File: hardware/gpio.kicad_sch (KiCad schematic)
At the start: 12 parts, among them J8 UART, J9 GPIO, Q4 BSN20

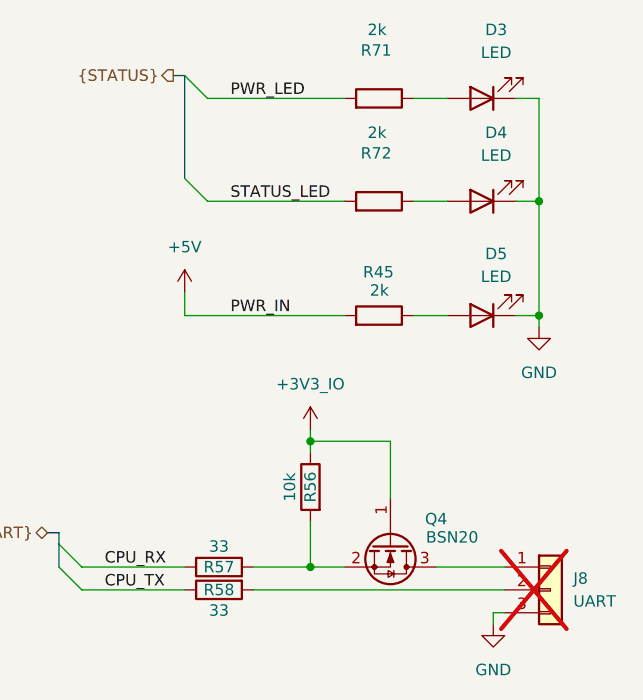
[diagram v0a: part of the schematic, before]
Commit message: Update crystal
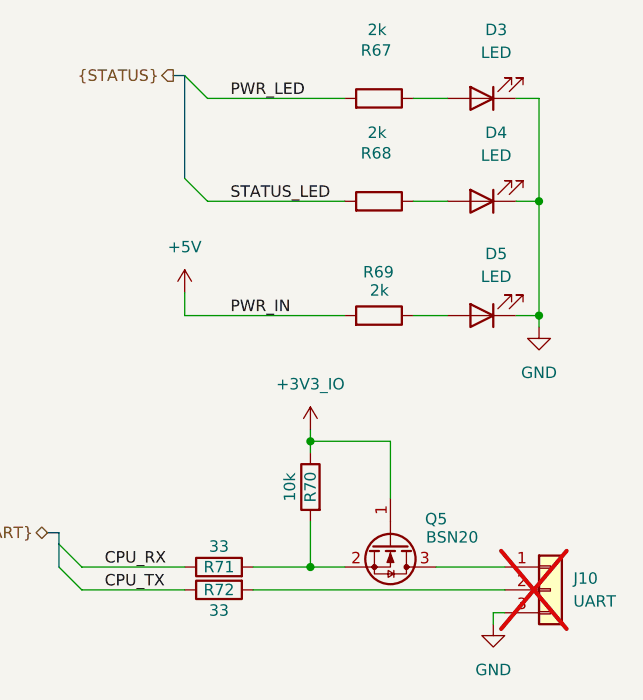
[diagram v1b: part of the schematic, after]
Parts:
- renumbered J8 to J10, Q4 to Q5, R71 to R67, R72 to R68, R45 to R69, R56 to R70, R57 to R71, R58 to R72
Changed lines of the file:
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@@
 		(on_board yes)
 		(dnp no)
-		(property "Reference" "R56"
+		(property "Reference" "R70"
 			(at 170.18 120.65 90)
 			(effects
@@
 			(project "cm0"
 				(path "/b53f5dbb-8078-4818-9e8f-fdf90ba6d854/452e4208-fdd2-4279-8880-491fefaabe1c"
-					(reference "R56")
+					(reference "R70")
 					(unit 1)
 				)
@@
 		(on_board yes)
 		(dnp no)
-		(property "Reference" "R72"
+		(property "Reference" "R68"
 			(at 175.768 83.566 90)
 			(effects
@@
 			(project "cm0"
 				(path "/b53f5dbb-8078-4818-9e8f-fdf90ba6d854/452e4208-fdd2-4279-8880-491fefaabe1c"
-					(reference "R72")
+					(reference "R68")
 					(unit 1)
 				)
@@
 		(on_board yes)
 		(dnp no)
-		(property "Reference" "R71"
+		(property "Reference" "R67"
 			(at 175.768 72.136 90)
 			(effects
@@
 			(project "cm0"
 				(path "/b53f5dbb-8078-4818-9e8f-fdf90ba6d854/452e4208-fdd2-4279-8880-491fefaabe1c"
-					(reference "R71")
+					(reference "R67")
 					(unit 1)
 				)
@@
 		(dnp no)
 		(fields_autoplaced yes)
-		(property "Reference" "#PWR0174"
+		(property "Reference" "#PWR0182"
 			(at 67.31 88.9 0)
 			(effects
@@
 			(project ""
 				(path "/b53f5dbb-8078-4818-9e8f-fdf90ba6d854/452e4208-fdd2-4279-8880-491fefaabe1c"
-					(reference "#PWR0174")
+					(reference "#PWR0182")
 					(unit 1)
 				)
@@
 		(dnp no)
 		(fields_autoplaced yes)
-		(property "Reference" "#PWR0172"
+		(property "Reference" "#PWR0188"
 			(at 82.55 142.24 0)
 			(effects
@@
 			(project ""
 				(path "/b53f5dbb-8078-4818-9e8f-fdf90ba6d854/452e4208-fdd2-4279-8880-491fefaabe1c"
-					(reference "#PWR0172")
+					(reference "#PWR0188")
 					(unit 1)
 				)
@@
 		(dnp no)
 		(fields_autoplaced yes)
-		(property "Reference" "#PWR0175"
+		(property "Reference" "#PWR0183"
 			(at 82.55 88.9 0)
 			(effects
@@
 			(project ""
 				(path "/b53f5dbb-8078-4818-9e8f-fdf90ba6d854/452e4208-fdd2-4279-8880-491fefaabe1c"
-					(reference "#PWR0175")
+					(reference "#PWR0183")
 					(unit 1)
 				)
@@
 		(on_board yes)
 		(dnp no)
-		(property "Reference" "R57"
+		(property "Reference" "R71"
 			(at 160.02 129.54 90)
 			(effects
@@
 			(project "cm0"
 				(path "/b53f5dbb-8078-4818-9e8f-fdf90ba6d854/452e4208-fdd2-4279-8880-491fefaabe1c"
-					(reference "R57")
+					(reference "R71")
 					(unit 1)
 				)
@@
 		(dnp no)
 		(fields_autoplaced yes)
-		(property "Reference" "#PWR0154"
+		(property "Reference" "#PWR0186"
 			(at 170.18 118.11 0)
 			(effects
@@
 			(project ""
 				(path "/b53f5dbb-8078-4818-9e8f-fdf90ba6d854/452e4208-fdd2-4279-8880-491fefaabe1c"
-					(reference "#PWR0154")
+					(reference "#PWR0186")
 					(unit 1)
 				)
@@
 		(on_board yes)
 		(dnp no)
-		(property "Reference" "R45"
+		(property "Reference" "R69"
 			(at 176.022 96.774 90)
 			(effects
@@
 			(project "cm0"
 				(path "/b53f5dbb-8078-4818-9e8f-fdf90ba6d854/452e4208-fdd2-4279-8880-491fefaabe1c"
-					(reference "R45")
+					(reference "R69")
 					(unit 1)
 				)
@@
 		(on_board yes)
 		(dnp no)
-		(property "Reference" "Q4"
+		(property "Reference" "Q5"
 			(at 184.15 124.206 90)
 			(effects
@@
 			(project "cm0"
 				(path "/b53f5dbb-8078-4818-9e8f-fdf90ba6d854/452e4208-fdd2-4279-8880-491fefaabe1c"
-					(reference "Q4")
+					(reference "Q5")
 					(unit 1)
 				)
@@
 		(dnp no)
 		(fields_autoplaced yes)
-		(property "Reference" "#PWR0155"
+		(property "Reference" "#PWR0189"
 			(at 190.5 142.24 0)
 			(effects
@@
 			(project ""
 				(path "/b53f5dbb-8078-4818-9e8f-fdf90ba6d854/452e4208-fdd2-4279-8880-491fefaabe1c"
-					(reference "#PWR0155")
+					(reference "#PWR0189")
 					(unit 1)
 				)
@@
 		(dnp no)
 		(fields_autoplaced yes)
-		(property "Reference" "#PWR019"
+		(property "Reference" "#PWR0185"
 			(at 195.58 109.22 0)
 			(effects
@@
 			(project ""
 				(path "/b53f5dbb-8078-4818-9e8f-fdf90ba6d854/452e4208-fdd2-4279-8880-491fefaabe1c"
-					(reference "#PWR019")
+					(reference "#PWR0185")
 					(unit 1)
 				)
@@
 		(dnp yes)
 		(fields_autoplaced yes)
-		(property "Reference" "J8"
+		(property "Reference" "J10"
 			(at 199.39 130.8099 0)
 			(effects
@@
 			(project ""
 				(path "/b53f5dbb-8078-4818-9e8f-fdf90ba6d854/452e4208-fdd2-4279-8880-491fefaabe1c"
-					(reference "J8")
+					(reference "J10")
 					(unit 1)
 				)
@@
 		(dnp no)
 		(fields_autoplaced yes)
-		(property "Reference" "#PWR0173"
+		(property "Reference" "#PWR0187"
 			(at 67.31 142.24 0)
 			(effects
@@
 			(project "cm0"
 				(path "/b53f5dbb-8078-4818-9e8f-fdf90ba6d854/452e4208-fdd2-4279-8880-491fefaabe1c"
-					(reference "#PWR0173")
+					(reference "#PWR0187")
 					(unit 1)
 				)
@@
 		(dnp no)
 		(fields_autoplaced yes)
-		(property "Reference" "#PWR0188"
+		(property "Reference" "#PWR0184"
 			(at 156.21 102.87 0)
 			(effects
@@
 			(project ""
 				(path "/b53f5dbb-8078-4818-9e8f-fdf90ba6d854/452e4208-fdd2-4279-8880-491fefaabe1c"
-					(reference "#PWR0188")
+					(reference "#PWR0184")
 					(unit 1)
 				)
@@
 		(on_board yes)
 		(dnp no)
-		(property "Reference" "R58"
+		(property "Reference" "R72"
 			(at 160.02 132.08 90)
 			(effects
@@
 			(project "cm0"
 				(path "/b53f5dbb-8078-4818-9e8f-fdf90ba6d854/452e4208-fdd2-4279-8880-491fefaabe1c"
-					(reference "R58")
-					(unit 1)
-				)
+					(reference "R72")
+					(unit 1)
+				)

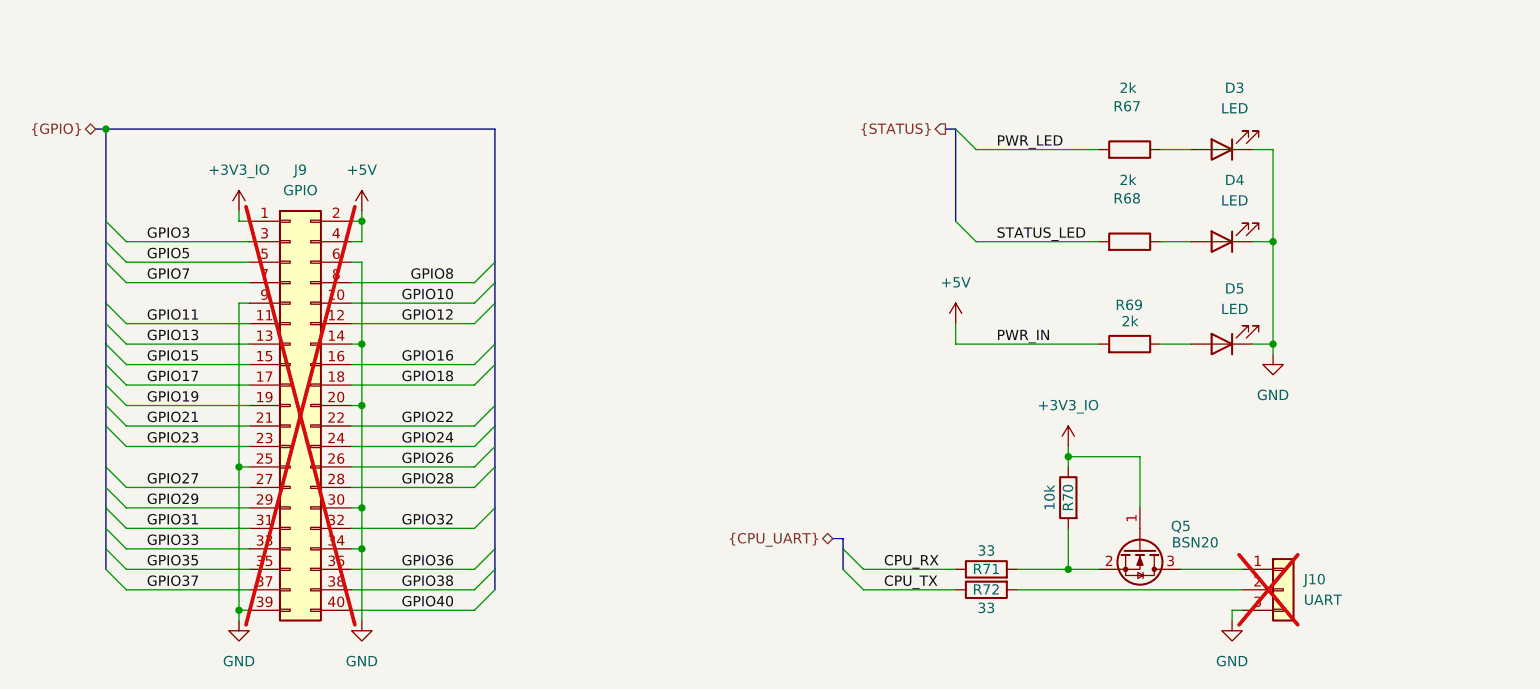
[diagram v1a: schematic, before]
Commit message: Add schematic pdf
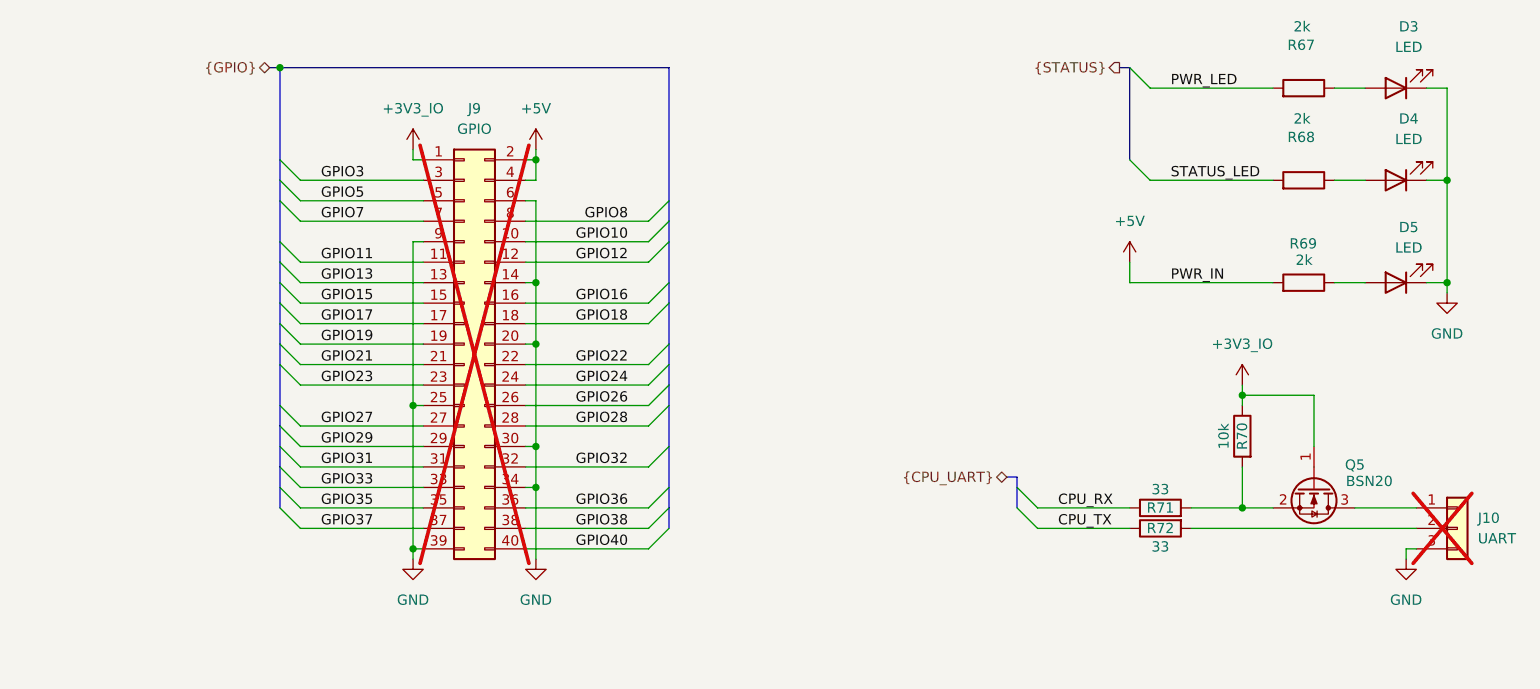
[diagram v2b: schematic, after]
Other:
- title: Icepi CM0 -> Icepi SBC
- moved on the sheet: D3, D4, D5, J10, J9, Q5, R67, R68, R69, R70, R71, R72
